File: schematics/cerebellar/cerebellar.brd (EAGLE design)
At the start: 98.4 x 91.1 mm, 67 parts, among them CON2 ODrive1, CON4 Odrive3, CON5 ODrive4, CON6 Odrive2, CON7 ODrive5, CON8 ODrive6, IC3 LTC7001, P1 Foot1, P10 SPI2, P11 Foot2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

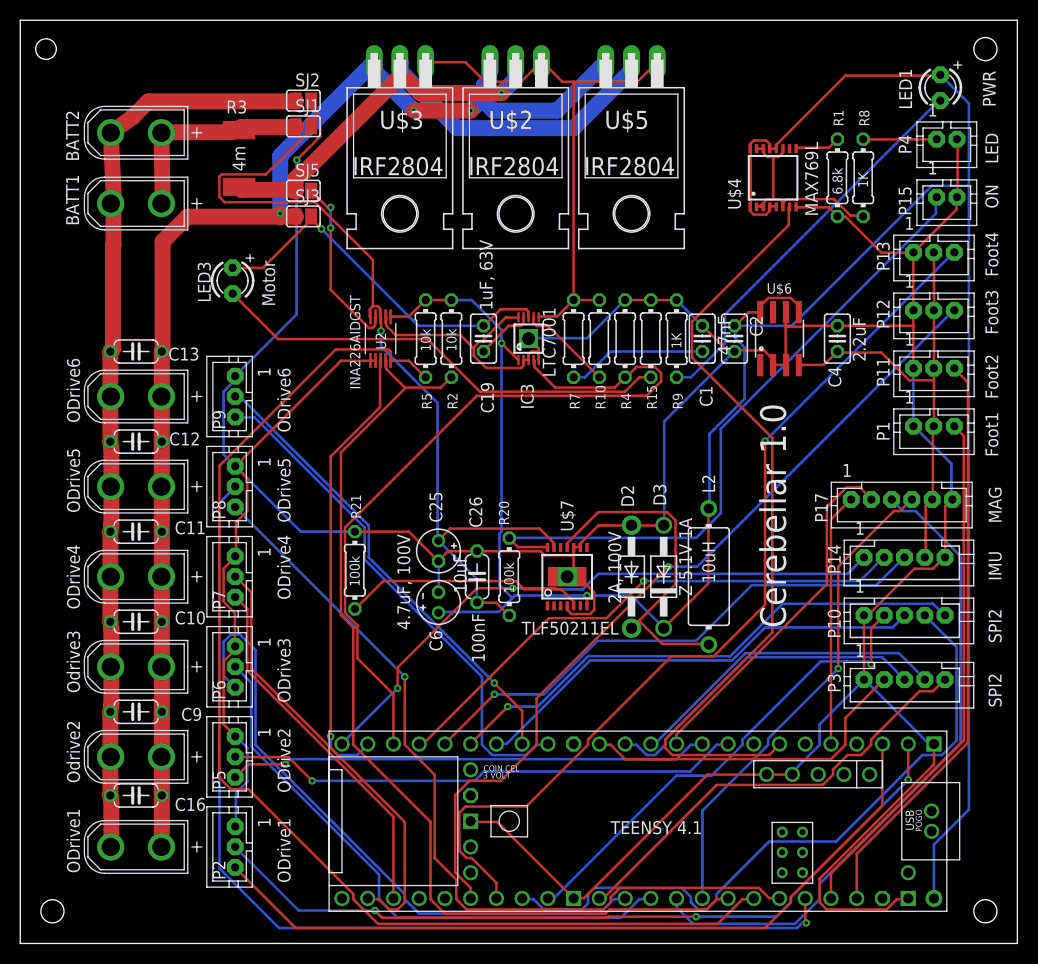
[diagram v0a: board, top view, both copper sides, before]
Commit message: Added Standby Line for 3.3. power supply
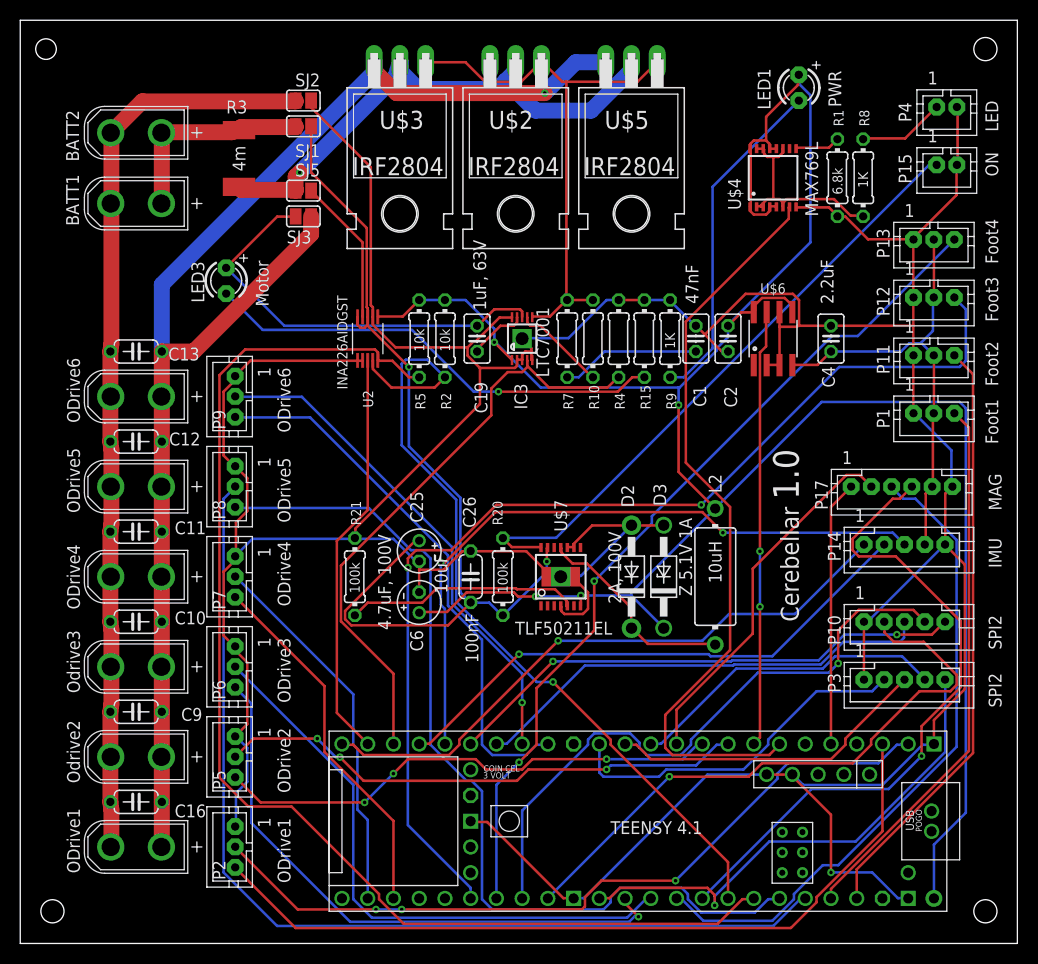
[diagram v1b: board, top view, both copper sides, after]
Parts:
- moved LED1 14.0 mm to (70.5, 84.5)
- moved P15 3.17 mm to (85.1, 76.8)
- moved P4 3.17 mm to (85.1, 82.5)
- moved C25 1.90 mm to (33.0, 38.7)
- moved C6 1.90 mm to (33.0, 33.7)
- moved P11 1.27 mm to (83.8, 56.5)
- moved P17 1.27 mm to (80.6, 45.1)
- moved U2 1.27 mm to (27.9, 59.7)
- moved P1 1.27 mm to (83.8, 50.8)
- moved P12 1.27 mm to (83.8, 62.2)
- moved P13 1.27 mm to (83.8, 67.9)
- moved P14 1.27 mm to (81.9, 39.4)
- moved C2 0.64 mm to (63.5, 59.7)
- moved C4 0.64 mm to (73.7, 59.7)
- moved R15 0.64 mm to (55.2, 59.7)
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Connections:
- new net N$8: U$1.6-OUT1D, U$6.7
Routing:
- net N$8: track 0.00 -> 43.2 mm, vias 0 -> 2
- net SENS3: track 82.6 -> 106.0 mm, vias 1 -> 2
- net +5V: track 255.5 -> 236.1 mm, vias 2 -> 4
- net N$10: track 76.5 -> 58.8 mm
- net MAG_SDA: track 48.3 -> 65.1 mm
- net N$22: track 95.9 -> 81.3 mm, vias 0 -> 1
- net T_RX: track 53.0 -> 67.2 mm, vias 1 -> 2
- net DRAIN: track 66.5 -> 53.5 mm
- net MISO1: track 47.4 -> 60.3 mm
- net N$42: track 33.1 -> 20.6 mm
- net GND: track 424.2 -> 436.2 mm
- net O5_TX: track 81.7 -> 90.3 mm, vias 1 -> 0
- net POWER+: track 125.4 -> 133.5 mm, vias 3 -> 1
- net SENS4: track 91.8 -> 85.2 mm, vias 1 -> 2
- net O4_RX: track 43.5 -> 37.2 mm
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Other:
- board text added: "1.0"
- board text added: "Cerebellar"
- board text removed: "Cerebellar 1.0"

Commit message: fixed socket of IMU layout
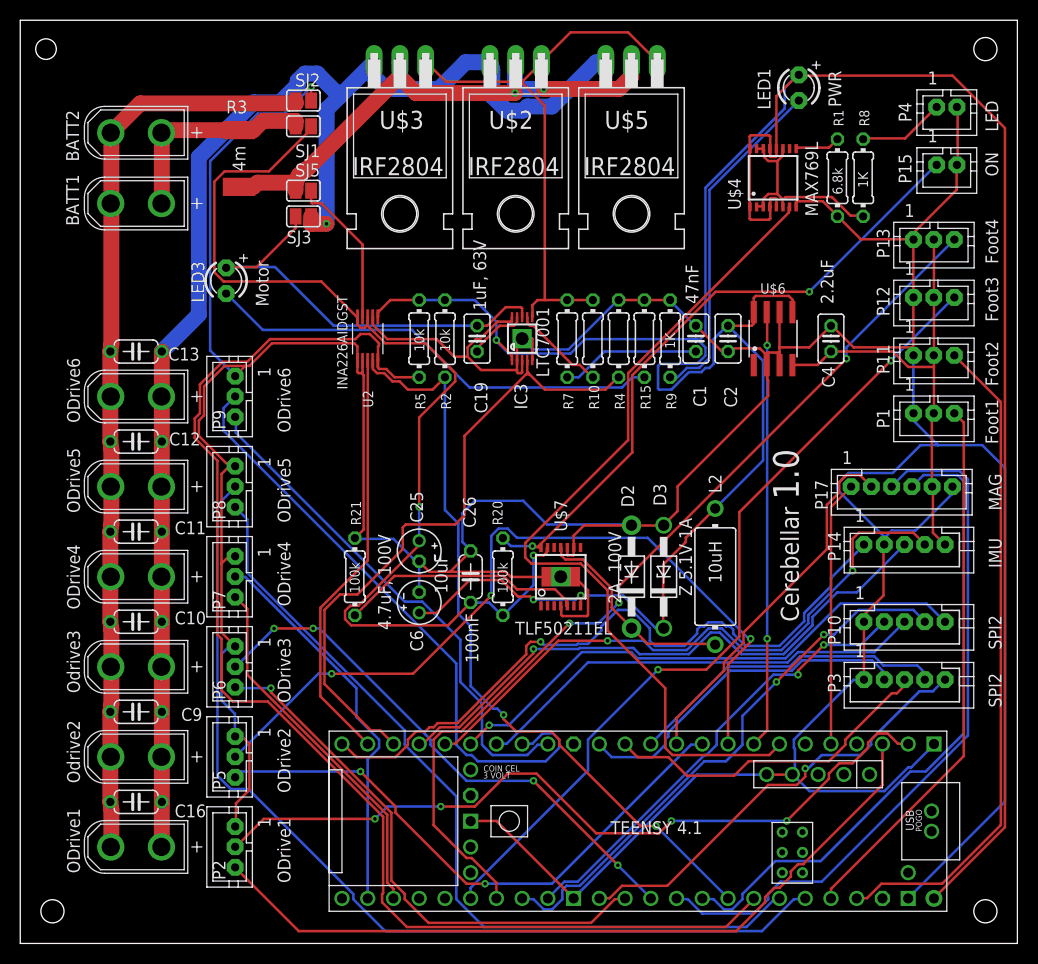
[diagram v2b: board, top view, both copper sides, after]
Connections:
- net T_RX renamed TXD
- removed net T_TX: P14.2, U$1.29-TX7
- new net RXD: P14.4, U$1.29-TX7
- net +3.3V: now also P14.5; no longer P14.4
- net GND: now also P14.2; no longer P14.5
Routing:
- net GND: track 436.2 -> 522.2 mm
- net RXD: track 0.00 -> 59.0 mm, vias 0 -> 1
- net +5V: track 236.1 -> 293.4 mm, vias 4 -> 3
- net T_TX: track 54.2 -> 0.00 mm, vias 1 -> 0
- net O2_RX: track 52.7 -> 79.5 mm
- net SENS3: track 106.0 -> 81.9 mm
- net MISO1: track 60.3 -> 45.5 mm, vias 1 -> 2
- net V+: track 92.4 -> 106.0 mm
- net O6_RX: track 49.9 -> 60.9 mm, vias 1 -> 0
- net LED_PWM: track 74.2 -> 84.9 mm
- net O5_TX: track 90.3 -> 82.0 mm
- net IMU_ENABLE: track 60.9 -> 69.1 mm
- net SENS4: track 85.2 -> 92.0 mm, vias 2 -> 3
- net POWER+: track 133.5 -> 140.2 mm
- net O2_TX: track 50.4 -> 57.0 mm, vias 3 -> 2
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
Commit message: Fusion with Magnetometer works
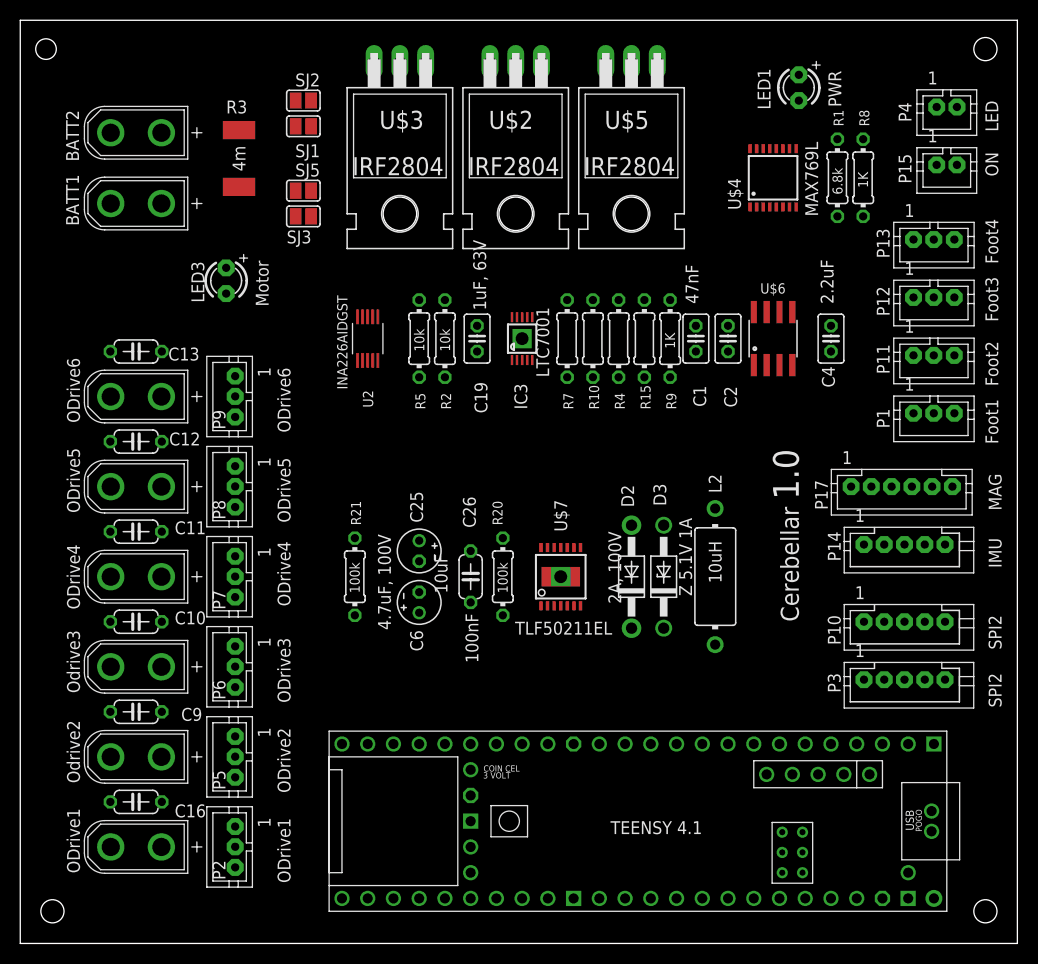
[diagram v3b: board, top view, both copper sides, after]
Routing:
- net GND: track 522.2 -> 0.00 mm, vias 1 -> 0
- net +5V: track 293.4 -> 0.00 mm, vias 3 -> 0
- net POWER+: track 140.2 -> 0.00 mm, vias 1 -> 0
- net N$17: track 127.0 -> 0.00 mm
- net V+: track 106.0 -> 0.00 mm, vias 2 -> 0
- net O5_RX: track 95.3 -> 0.00 mm
- net SENS4: track 92.0 -> 0.00 mm, vias 3 -> 0
- net BATT-: track 90.5 -> 0.00 mm
- net LED_PWM: track 84.9 -> 0.00 mm
- net O5_TX: track 82.0 -> 0.00 mm
- net SENS3: track 81.9 -> 0.00 mm, vias 2 -> 0
- net O2_RX: track 79.5 -> 0.00 mm, vias 3 -> 0
- net O1_TX: track 77.1 -> 0.00 mm
- net O1_RX: track 77.0 -> 0.00 mm, vias 4 -> 0
- net N$22: track 75.5 -> 0.00 mm, vias 2 -> 0
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
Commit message: Fixed hard iron magnetometer
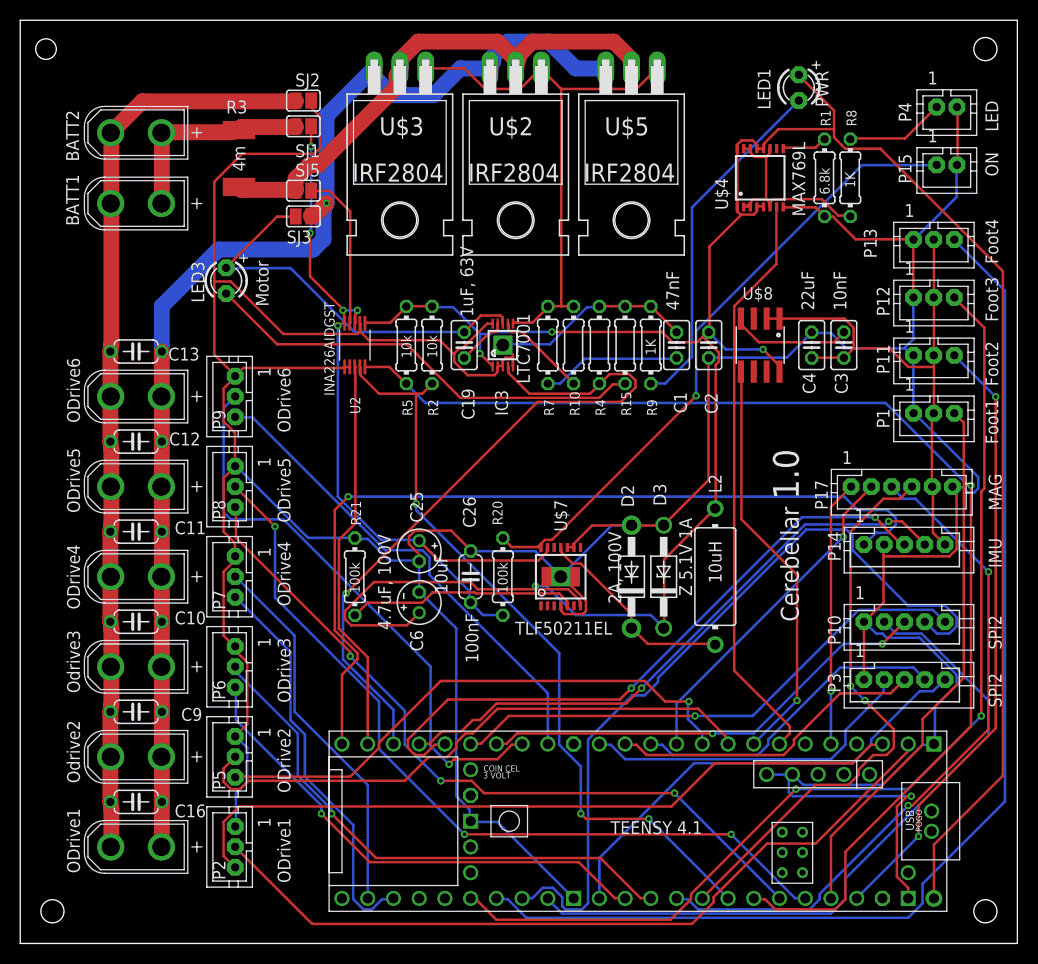
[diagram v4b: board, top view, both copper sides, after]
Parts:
- removed U$6: MAX884, MAX884:SO08
- added C3: 10nF, rcl:C025-025X050
- added U$8: LT1763, LT1763:SO08
- C4: value 2.2uF -> 22uF
- moved C1 2.01 mm to (58.4, 59.1)
- moved C2 2.01 mm to (61.6, 59.1)
- moved C4 2.01 mm to (71.8, 59.1)
- moved IC3 2.01 mm to (41.3, 59.1)
- moved R10 2.01 mm to (48.3, 59.1)
- moved R4 2.01 mm to (50.8, 59.1)
- moved R7 2.01 mm to (45.7, 59.1)
- moved R15 2.01 mm to (53.3, 59.1)
- moved R9 2.01 mm to (55.9, 59.1)
- moved R2 1.42 mm to (34.3, 59.1)
- moved R5 1.42 mm to (31.8, 59.1)
- moved U2 1.42 mm to (26.7, 59.1)
- moved C19 1.42 mm to (37.5, 59.1)
- moved R1 1.27 mm to (73.0, 75.6)
- moved R8 1.27 mm to (75.6, 75.6)
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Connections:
- new net N$9: U$1.6-OUT1D, U$8.5
- net +3.3V: now also C3.1, U$8.1, U$8.2; no longer U$6.4
- net +5V: now also U$8.8; no longer U$6.5, U$6.8
- net GND: no longer U$6.2, U$6.3, U$6.6
- net N$8: now also C3.2, U$8.4; no longer U$1.6-OUT1D, U$6.7
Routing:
- net GND: track 0.00 -> 463.9 mm, vias 0 -> 1
- net +5V: track 0.00 -> 258.9 mm, vias 0 -> 4
- net POWER+: track 0.00 -> 121.3 mm, vias 0 -> 1
- net N$17: track 0.00 -> 120.6 mm, vias 0 -> 1
- net SENS4: track 0.00 -> 114.4 mm
- net SENS3: track 0.00 -> 102.6 mm, vias 0 -> 2
- net BATT-: track 0.00 -> 90.4 mm
- net IMU_ENABLE: track 0.00 -> 86.0 mm, vias 0 -> 1
- net O5_RX: track 0.00 -> 80.0 mm, vias 0 -> 3
- net CS1: track 0.00 -> 79.2 mm
- net O1_RX: track 0.00 -> 77.6 mm
- net V+: track 0.00 -> 77.3 mm, vias 0 -> 5
- net N$22: track 0.00 -> 75.3 mm, vias 0 -> 3
- net O5_TX: track 0.00 -> 73.7 mm, vias 0 -> 3
- net O1_TX: track 0.00 -> 73.2 mm
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
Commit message: new power supply
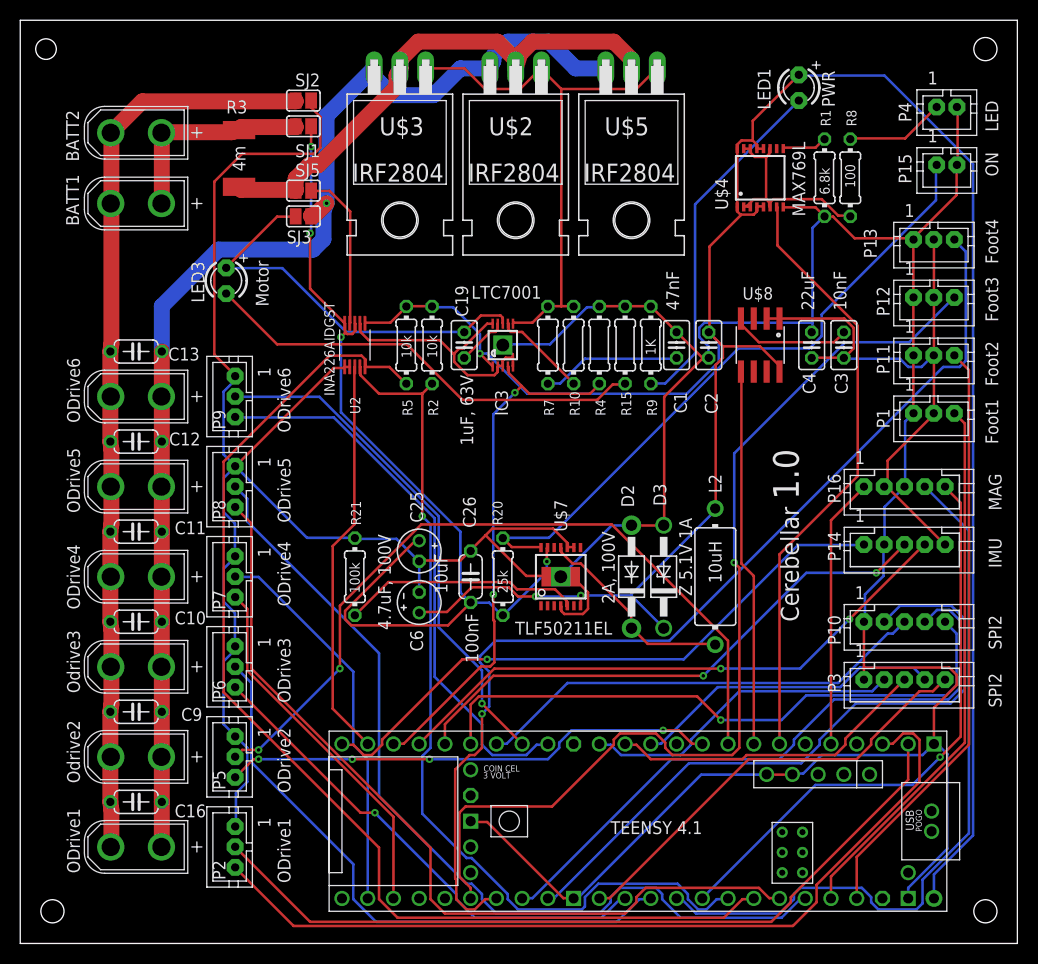
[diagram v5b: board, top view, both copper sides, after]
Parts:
- removed P17: MAG, jst-ph:JST-PH6
- added P16: MAG, jst-ph:JST-PH5
- R20: value 100k -> 25k
- R8: value 1K -> 100
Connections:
- net +3.3V: now also P16.2; no longer P17.5
- net GND: now also P16.3; no longer P17.6
- net MAG_EN: no longer P17.2
- net MAG_INT: now also P16.1; no longer P17.1
- net MAG_SCL: now also P16.4; no longer P17.3
- net MAG_SDA: now also P16.5; no longer P17.4
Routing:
- net MAG_EN: track 33.4 -> 0.00 mm, vias 1 -> 0
- net GND: track 463.9 -> 435.8 mm, vias 1 -> 0
- net IMU_ENABLE: track 86.0 -> 60.9 mm
- net O2_RX: track 58.4 -> 76.7 mm, vias 0 -> 2
- net +5V: track 258.9 -> 241.6 mm, vias 4 -> 3
- net N$10: track 69.9 -> 52.7 mm, vias 1 -> 2
- net CS1: track 79.2 -> 63.2 mm
- net V+: track 77.3 -> 92.8 mm, vias 5 -> 4
- net N$22: track 75.3 -> 89.1 mm, vias 3 -> 1
- net O1_TX: track 73.2 -> 85.4 mm
- net SENS4: track 114.4 -> 103.4 mm, vias 0 -> 1
- net TXD: track 64.5 -> 54.7 mm
- net O5_TX: track 73.7 -> 83.5 mm, vias 3 -> 0
- net SCK1: track 52.8 -> 61.3 mm
- net N$17: track 120.6 -> 112.1 mm, vias 1 -> 0
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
